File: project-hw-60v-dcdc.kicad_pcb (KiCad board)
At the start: 2 copper layers, 25 x 20 mm, 17 parts, among them J1 Conn_01x01_Socket, J2 Conn_01x01_Socket, J3 Conn_01x01_Socket, J4 Conn_01x01_Socket, Q1 Q_Toshiba_SSM3J351R, U1 LMR516x5

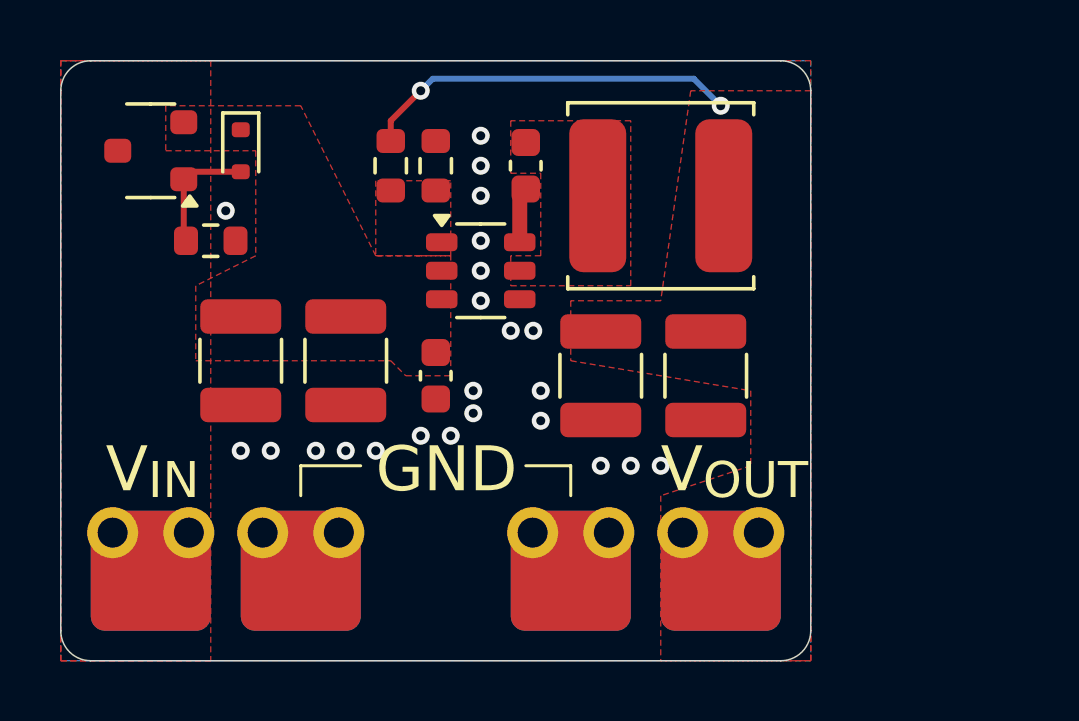
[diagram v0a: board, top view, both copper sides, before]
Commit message: pcb: set board edge closer to golden pads
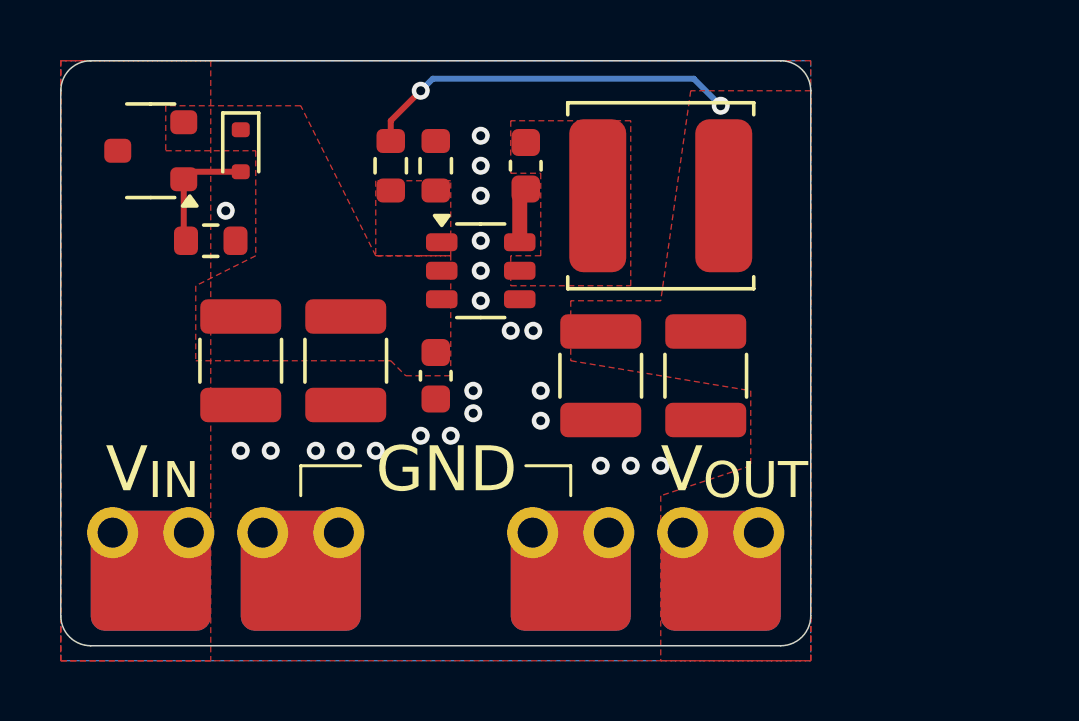
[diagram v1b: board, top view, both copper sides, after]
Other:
- board size 25 x 20 mm -> 25 x 19.5 mm
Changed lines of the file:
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@@
 	(gr_line
 		(start 59 23)
-		(end 59 41)
+		(end 59 40.5)
 		(stroke
 			(width 0.05)
@@
 	)
 	(gr_arc
-		(start 59 41)
-		(mid 58.707107 41.707107)
-		(end 58 42)
+		(start 59 40.5)
+		(mid 58.707107 41.207107)
+		(end 58 41.5)
 		(stroke
 			(width 0.05)
@@
 	)
 	(gr_line
-		(start 34 41)
+		(start 34 40.5)
 		(end 34 23)
 		(stroke
@@
 	)
 	(gr_arc
-		(start 35 42)
-		(mid 34.292893 41.707107)
-		(end 34 41)
+		(start 35 41.5)
+		(mid 34.292893 41.207107)
+		(end 34 40.5)
 		(stroke
 			(width 0.05)
@@
 	)
 	(gr_line
-		(start 58 42)
-		(end 35 42)
+		(start 58 41.5)
+		(end 35 41.5)
 		(stroke
 			(width 0.05)

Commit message: pcb: add version
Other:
- board text added: "v1.0.0"
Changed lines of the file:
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@@
 		(layer "Edge.Cuts")
+	)
+	(gr_text "v1.0.0"
+		(at 41 25 0)
+		(layer "B.SilkS")
+		(effects
+			(font
+				(face "FreeSans")
+				(size 1.5 1.5)
+				(thickness 0.1)
+			)
+			(justify left bottom mirror)
+		)
+		(render_cache "v1.0.0" 0
+			(polygon
+				(pts
+					(xy 40.398429 24.745) (xy 40.590771 24.745) (xy 40.97875 23.642976) (xy 40.780547 23.642976) (xy 40.485258 24.536905)
+					(xy 40.172749 23.642976) (xy 39.974546 23.642976)
+				)
+			)
+			(polygon
+				(pts
+					(xy 39.412909 23.666423) (xy 39.744103 23.666423) (xy 39.744103 23.525739) (xy 39.668712 23.515289)
+					(xy 39.594039 23.501339) (xy 39.519052 23.480622) (xy 39.463468 23.453932) (xy 39.413026 23.397253)
+					(xy 39.378093 23.327158) (xy 39.352568 23.254492) (xy 39.349528 23.244371) (xy 39.227163 23.244371)
+					(xy 39.227163 24.745) (xy 39.412909 24.745)
+				)
+			)
+			(polygon
+				(pts
+					(xy 38.404675 24.533974) (xy 38.404675 24.745) (xy 38.624127 24.745) (xy 38.624127 24.533974)
+				)
+			)
+			(polygon
+				(pts
+					(xy 37.747572 23.247597) (xy 37.819958 23.261224) (xy 37.88758 23.288643) (xy 37.949651 23.328635)
+					(xy 37.97026 23.345072) (xy 38.023114 23.399087) (xy 38.065788 23.459794) (xy 38.068794 23.464892)
+					(xy 38.10236 23.53556) (xy 38.126789 23.607831) (xy 38.146022 23.683276) (xy 38.149837 23.701308)
+					(xy 38.162637 23.77687) (xy 38.171498 23.857929) (xy 38.176021 23.933362) (xy 38.177529 24.013004)
+					(xy 38.177408 24.03664) (xy 38.174488 24.127627) (xy 38.167676 24.212924) (xy 38.156971 24.292531)
+					(xy 38.142374 24.366448) (xy 38.118653 24.450842) (xy 38.08885 24.526346) (xy 38.052965 24.592958)
+					(xy 38.036943 24.617048) (xy 37.983448 24.679993) (xy 37.921813 24.72895) (xy 37.852037 24.763919)
+					(xy 37.774122 24.7849) (xy 37.688066 24.791894) (xy 37.658696 24.791126) (xy 37.57589 24.779598)
+					(xy 37.501045 24.754237) (xy 37.434159 24.715043) (xy 37.375233 24.662017) (xy 37.324267 24.595157)
+					(xy 37.316536 24.582666) (xy 37.281561 24.515073) (xy 37.252722 24.438911) (xy 37.23002 24.35418)
+					(xy 37.216275 24.280226) (xy 37.206458 24.200788) (xy 37.200567 24.115866) (xy 37.198604 24.02546)
+					(xy 37.198945 24.008607) (xy 37.388381 24.008607) (xy 37.389537 24.085246) (xy 37.394234 24.173767)
+					(xy 37.402546 24.254203) (xy 37.41447 24.326553) (xy 37.43355 24.402699) (xy 37.462386 24.476821)
+					(xy 37.492912 24.528118) (xy 37.549616 24.585163) (xy 37.619419 24.618329) (xy 37.692463 24.627763)
+					(xy 37.777532 24.612799) (xy 37.848182 24.567907) (xy 37.894321 24.510445) (xy 37.931232 24.433829)
+					(xy 37.95286 24.363797) (xy 37.969297 24.282991) (xy 37.980543 24.191411) (xy 37.986599 24.089057)
+					(xy 37.987752 24.014836) (xy 37.98746 23.977532) (xy 37.98307 23.872726) (xy 37.973412 23.778579)
+					(xy 37.958486 23.69509) (xy 37.930391 23.60035) (xy 37.89293 23.524559) (xy 37.846104 23.467715)
+					(xy 37.774402 23.423306) (xy 37.688066 23.408503) (xy 37.651776 23.410847) (xy 37.571294 23.437219)
+					(xy 37.505445 23.492892) (xy 37.463302 23.558529) (xy 37.430524 23.642919) (xy 37.412086 23.718518)
+					(xy 37.398916 23.804665) (xy 37.391014 23.901362) (xy 37.388381 24.008607) (xy 37.198945 24.008607)
+					(xy 37.200516 23.930875) (xy 37.206252 23.842392) (xy 37.215811 23.760012) (xy 37.229195 23.683734)
+					(xy 37.256441 23.580758) (xy 37.29229 23.491513) (xy 37.336743 23.415997) (xy 37.3898 23.354212)
+					(xy 37.451461 23.306157) (xy 37.521726 23.271832) (xy 37.600594 23.251236) (xy 37.688066 23.244371)
+				)
+			)
+			(polygon
+				(pts
+					(xy 36.713538 24.533974) (xy 36.713538 24.745) (xy 36.93299 24.745) (xy 36.93299 24.533974)
+				)
+			)
+			(polygon
+				(pts
+					(xy 36.056435 23.247597) (xy 36.12882 23.261224) (xy 36.196442 23.288643) (xy 36.258513 23.328635)
+					(xy 36.279123 23.345072) (xy 36.331977 23.399087) (xy 36.374651 23.459794) (xy 36.377657 23.464892)
+					(xy 36.411222 23.53556) (xy 36.435651 23.607831) (xy 36.454884 23.683276) (xy 36.4587 23.701308)
+					(xy 36.4715 23.77687) (xy 36.480361 23.857929) (xy 36.484884 23.933362) (xy 36.486392 24.013004)
+					(xy 36.48627 24.03664) (xy 36.483351 24.127627) (xy 36.476538 24.212924) (xy 36.465834 24.292531)
+					(xy 36.451236 24.366448) (xy 36.427516 24.450842) (xy 36.397713 24.526346) (xy 36.361828 24.592958)
+					(xy 36.345805 24.617048) (xy 36.29231 24.679993) (xy 36.230675 24.72895) (xy 36.1609 24.763919)
+					(xy 36.082985 24.7849) (xy 35.996929 24.791894) (xy 35.967558 24.791126) (xy 35.884753 24.779598)
+					(xy 35.809907 24.754237) (xy 35.743021 24.715043) (xy 35.684095 24.662017) (xy 35.633129 24.595157)
+					(xy 35.625398 24.582666) (xy 35.590424 24.515073) (xy 35.561585 24.438911) (xy 35.538882 24.35418)
+					(xy 35.525138 24.280226) (xy 35.51532 24.200788) (xy 35.50943 24.115866) (xy 35.507466 24.02546)
+					(xy 35.507807 24.008607) (xy 35.697243 24.008607) (xy 35.698399 24.085246) (xy 35.703097 24.173767)
+					(xy 35.711408 24.254203) (xy 35.723333 24.326553) (xy 35.742412 24.402699) (xy 35.771249 24.476821)
+					(xy 35.801774 24.528118) (xy 35.858478 24.585163) (xy 35.928282 24.618329) (xy 36.001325 24.627763)
+					(xy 36.086394 24.612799) (xy 36.157045 24.567907) (xy 36.203184 24.510445) (xy 36.240095 24.433829)
+					(xy 36.261722 24.363797) (xy 36.278159 24.282991) (xy 36.289406 24.191411) (xy 36.295462 24.089057)
+					(xy 36.296615 24.014836) (xy 36.296322 23.977532) (xy 36.291932 23.872726) (xy 36.282275 23.778579)
+					(xy 36.267349 23.69509) (xy 36.239253 23.60035) (xy 36.201792 23.524559) (xy 36.154967 23.467715)
+					(xy 36.083264 23.423306) (xy 35.996929 23.408503) (xy 35.960639 23.410847) (xy 35.880157 23.437219)
+					(xy 35.814308 23.492892) (xy 35.772165 23.558529) (xy 35.739386 23.642919) (xy 35.720949 23.718518)
+					(xy 35.707779 23.804665) (xy 35.699877 23.901362) (xy 35.697243 24.008607) (xy 35.507807 24.008607)
+					(xy 35.509378 23.930875) (xy 35.515114 23.842392) (xy 35.524674 23.760012) (xy 35.538058 23.683734)
+					(xy 35.565303 23.580758) (xy 35.601153 23.491513) (xy 35.645606 23.415997) (xy 35.698663 23.354212)
+					(xy 35.760324 23.306157) (xy 35.830588 23.271832) (xy 35.909457 23.251236) (xy 35.996929 23.244371)
+				)
+			)
+		)
 	)
 	(gr_text "GND"

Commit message: pcb: change tolerances to 0.25 mm
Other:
- board size 25 x 19.5 mm -> 25 x 20 mm

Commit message: pcb: update pcb version
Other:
- board text added: "v1.0.0-2-gc3377dc"
- board text removed: "v1.0.0"

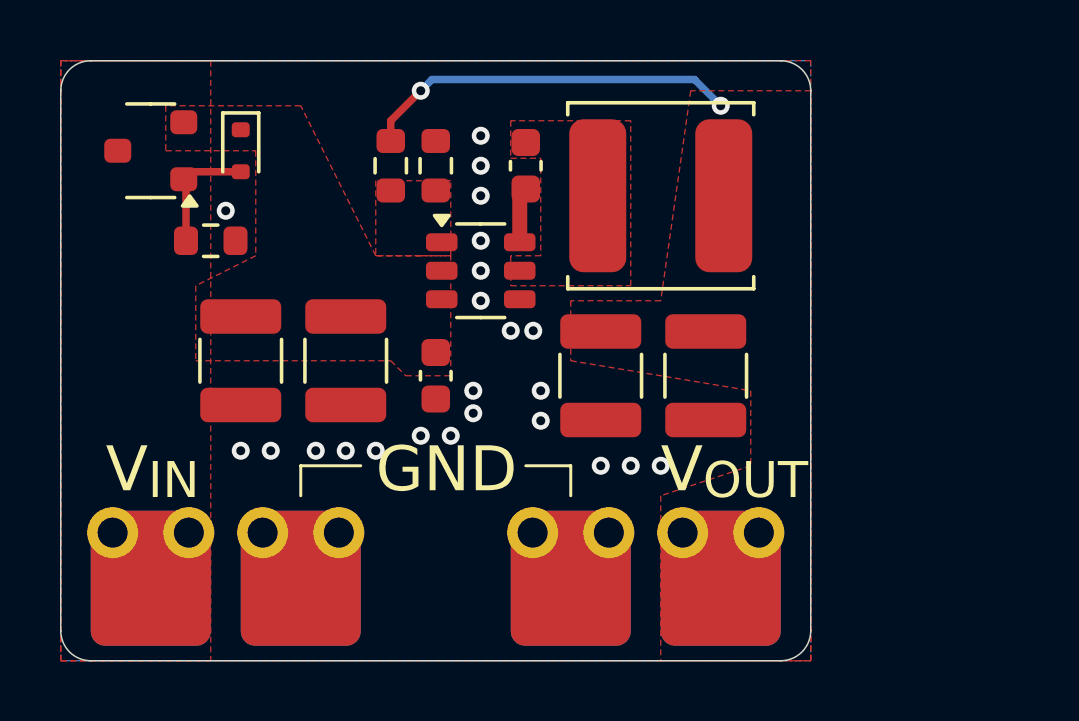
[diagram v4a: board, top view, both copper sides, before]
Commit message: pcb: make board 1 mm larger on the right
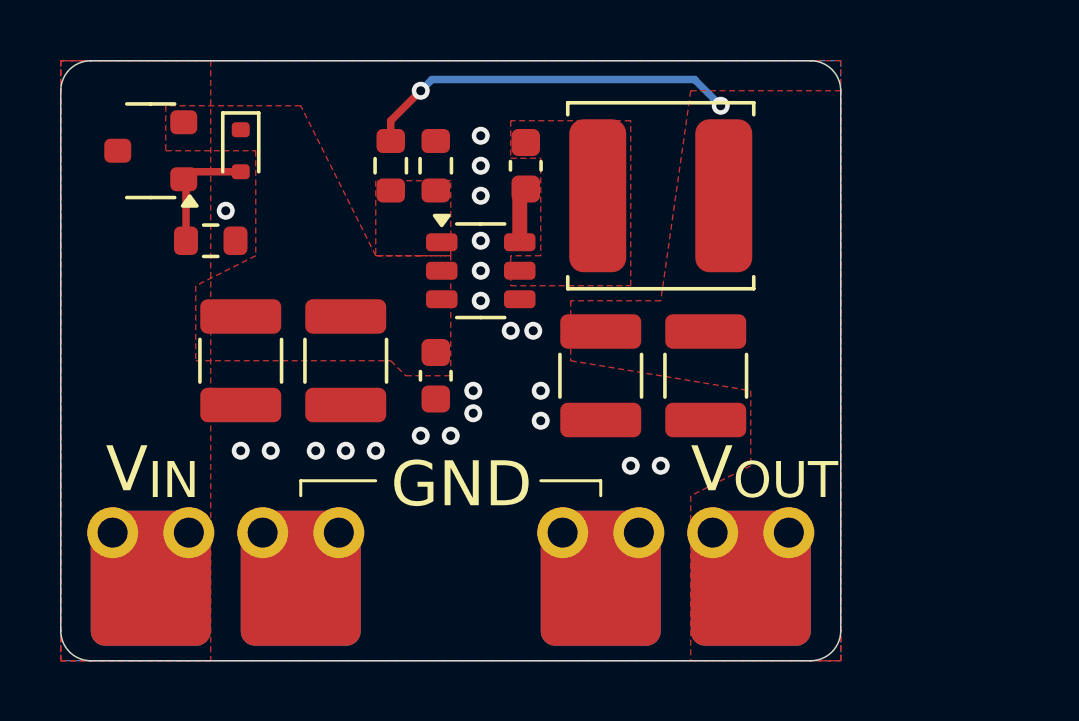
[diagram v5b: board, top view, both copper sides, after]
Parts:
- moved J3 1.00 mm to (57.0, 39.0)
- moved J4 1.00 mm to (52.0, 39.0)
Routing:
- net GND: vias 23 -> 22
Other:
- board size 25 x 20 mm -> 26 x 20 mm

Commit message: pcb: update version
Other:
- board text added: "v1.0.0-5-g07f53f4"
- board text removed: "v1.0.0-2-gc3377dc"
